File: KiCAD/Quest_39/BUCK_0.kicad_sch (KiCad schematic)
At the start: 26 parts, among them U4 AD626ANZ, U5 INA226, U6 LTM4611EV-PBF, U7 MCP4151-502E/SN

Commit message: Small changes made during schematic review w/ Joost
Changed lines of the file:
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@@
   (junction (at 322.58 137.16) (diameter 0) (color 0 0 0 0)
   )
-  (junction (at 322.58 180.34) (diameter 0) (color 0 0 0 0)
-  )
   (junction (at 236.22 215.9) (diameter 0) (color 0 0 0 0)
   )
@@
   (junction (at 166.37 50.8) (diameter 0) (color 0 0 0 0)
   )
-  (junction (at 322.58 68.58) (diameter 0) (color 0 0 0 0)
-  )
   (junction (at 322.58 101.6) (diameter 0) (color 0 0 0 0)
   )
@@
   )
   (junction (at 241.3 215.9) (diameter 0) (color 0 0 0 0)
-  )
-  (junction (at 162.56 215.9) (diameter 0) (color 0 0 0 0)
   )
   (junction (at 200.66 215.9) (diameter 0) (color 0 0 0 0)
@@
     (stroke (width 0) (type default) (color 0 0 0 0))
   )
-  (wire (pts (xy 322.58 68.58) (xy 322.58 66.04))
-    (stroke (width 0) (type default) (color 0 0 0 0))
-  )
   (wire (pts (xy 25.4 69.85) (xy 62.23 69.85))
     (stroke (width 0) (type default) (color 0 0 0 0))
@@
     (stroke (width 0) (type default) (color 0 0 0 0))
   )
-  (wire (pts (xy 322.58 180.34) (xy 322.58 177.8))
+  (wire (pts (xy 130.81 152.4) (xy 130.81 154.94))
     (stroke (width 0) (type default) (color 0 0 0 0))
   )
@@
     (stroke (width 0) (type default) (color 0 0 0 0))
   )
-  (wire (pts (xy 130.81 215.9) (xy 162.56 215.9))
-    (stroke (width 0) (type default) (color 0 0 0 0))
-  )
   (wire (pts (xy 322.58 132.08) (xy 322.58 134.62))
     (stroke (width 0) (type default) (color 0 0 0 0))
@@
     (stroke (width 0) (type default) (color 0 0 0 0))
   )
-  (wire (pts (xy 356.87 215.9) (xy 397.51 215.9))
+  (wire (pts (xy 356.87 215.9) (xy 400.05 215.9))
     (stroke (width 0) (type default) (color 0 0 0 0))
   )
@@
     (stroke (width 0) (type default) (color 0 0 0 0))
   )
+  (wire (pts (xy 130.81 154.94) (xy 129.54 154.94))
+    (stroke (width 0) (type default) (color 0 0 0 0))
+  )
   (wire (pts (xy 271.78 215.9) (xy 269.24 215.9))
     (stroke (width 0) (type default) (color 0 0 0 0))
@@
     (stroke (width 0) (type default) (color 0 0 0 0))
   )
-  (wire (pts (xy 130.81 152.4) (xy 130.81 215.9))
-    (stroke (width 0) (type default) (color 0 0 0 0))
-  )
   (polyline (pts (xy 351.79 219.71) (xy 278.13 219.71))
     (stroke (width 0) (type default) (color 0 0 0 0))
@@
     (stroke (width 0) (type default) (color 0 0 0 0))
   )
-  (wire (pts (xy 396.24 172.72) (xy 397.51 172.72))
+  (wire (pts (xy 396.24 172.72) (xy 400.05 172.72))
     (stroke (width 0) (type default) (color 0 0 0 0))
   )
@@
     (effects (font (size 1.27 1.27)) (justify left))
   )
-  (hierarchical_label "NEG" (shape output) (at 397.51 215.9 0)
+  (hierarchical_label "NEG" (shape output) (at 400.05 215.9 0)
     (effects (font (size 1.27 1.27)) (justify left))
+  )
+  (hierarchical_label "NEG" (shape output) (at 129.54 154.94 180)
+    (effects (font (size 1.27 1.27)) (justify right))
   )
   (hierarchical_label "SCK" (shape input) (at 285.75 232.41 180)
@@
     (effects (font (size 1.27 1.27)) (justify right))
   )
-  (hierarchical_label "POS" (shape output) (at 397.51 172.72 0)
+  (hierarchical_label "POS" (shape output) (at 400.05 172.72 0)
     (effects (font (size 1.27 1.27)) (justify left))
   )

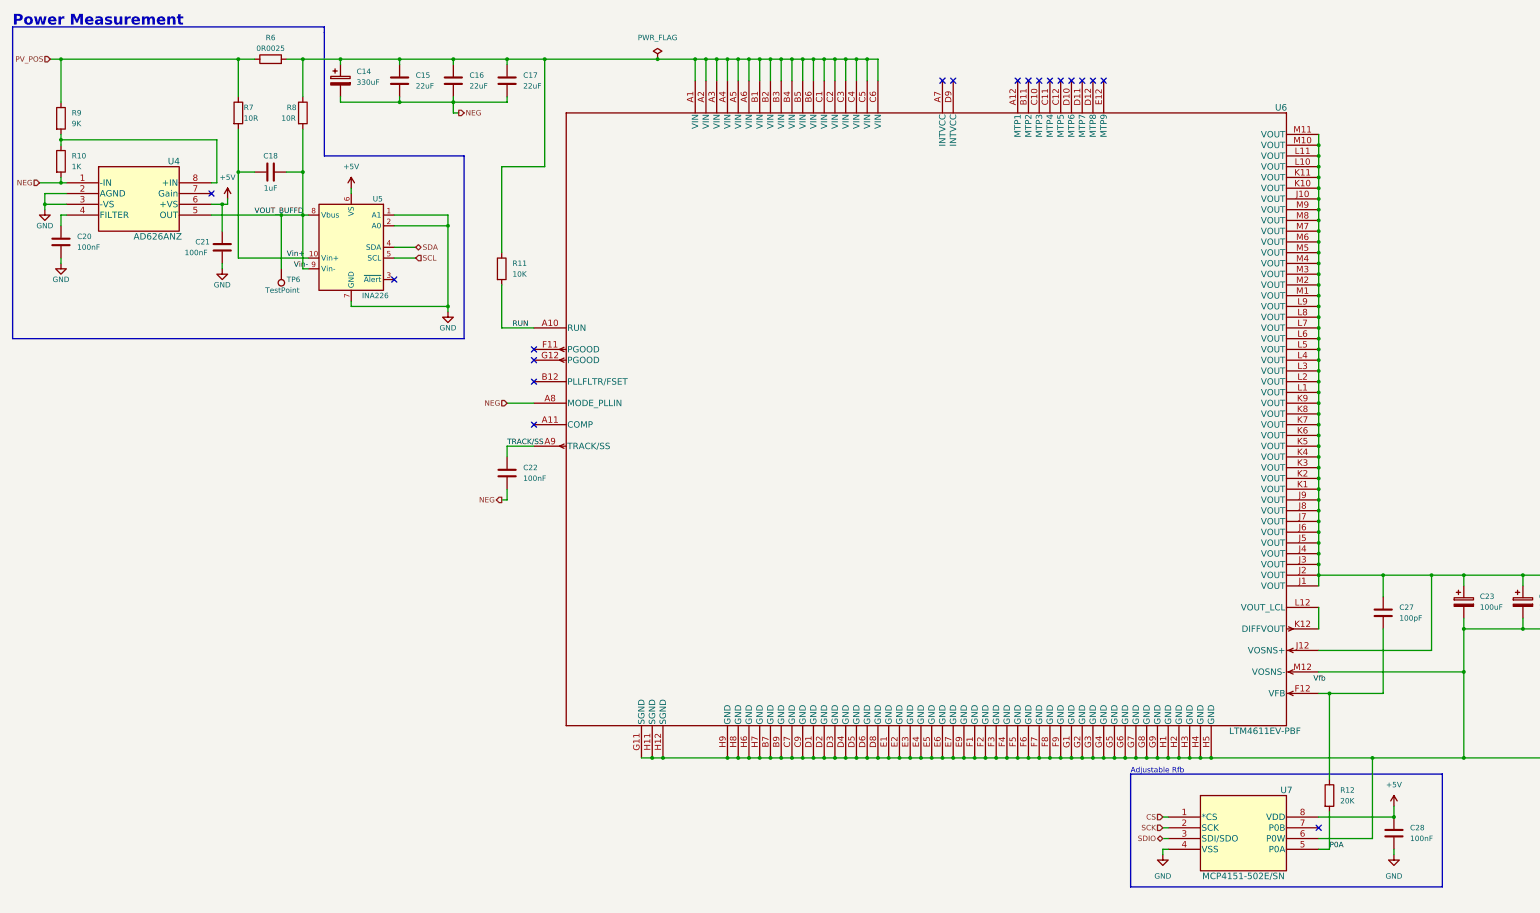
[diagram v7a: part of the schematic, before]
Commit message: Added weak SPI CS pullups to prevent spurious behaviour
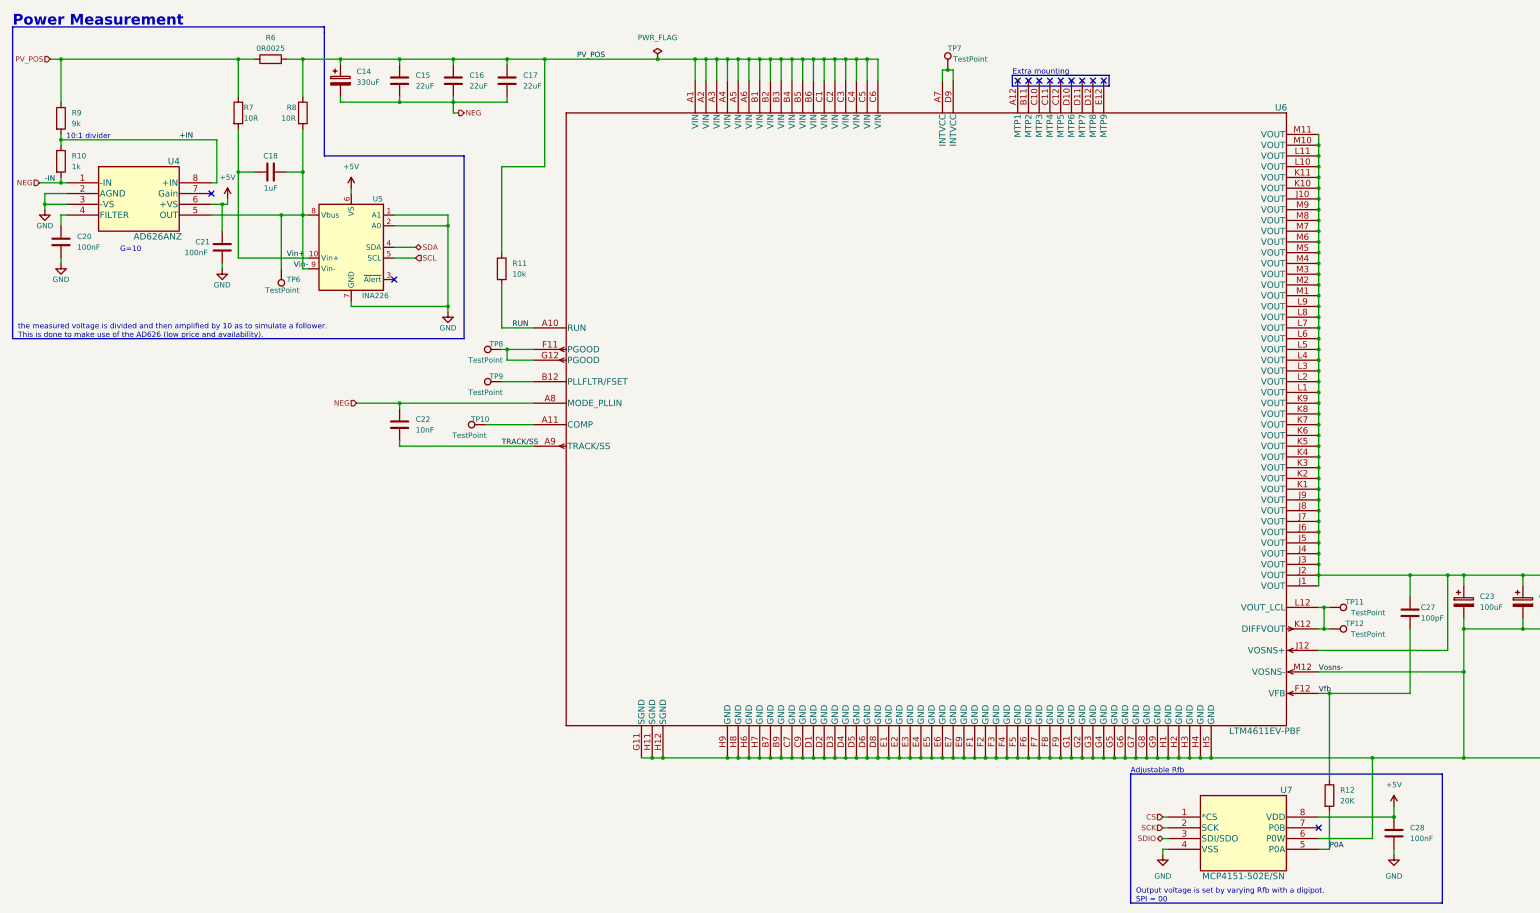
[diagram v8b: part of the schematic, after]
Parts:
- added TP10, TP11, TP12, TP7, TP8, TP9: TestPoint, symbol Connector:TestPoint
- C22: value 100nF -> 10nF
- R10: value 1K -> 1k
- R11: value 10K -> 10k
- R9: value 9K -> 9k
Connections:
- net NEG: now also C22.1; no longer C22.2
- net PV_POS: now also C14.1, C15.1, C16.1, C17.1, R11.1, R6.2, R8.1, U6.A1 (VIN), U6.A2 (VIN), U6.A3 (VIN), U6.A4 (VIN), U6.A5 (VIN), U6.A6 (VIN), U6.B1 (VIN), U6.B2 (VIN), U6.B3 (VIN), U6.B4 (VIN), U6.B5 (VIN), U6.B6 (VIN), U6.C1 (VIN), U6.C2 (VIN), U6.C3 (VIN), U6.C4 (VIN), U6.C5 (VIN), U6.C6 (VIN)
- net TRACK/SS: now also C22.2; no longer C22.1
- net Vfb: now also C27.2, R12.1, U6.F12 (VFB)
- net +IN: now reaches R10.1, R9.2, U4.8 (+IN)
- net at U6.A11 (COMP): now also TP10.1
- net at U6.A7 (INTVCC): now also U6.D9 (INTVCC), TP7.1
- net at U6.B12 (PLLFLTR/FSET): now also TP9.1
- net at U6.F11 (PGOOD): now also U6.G12 (PGOOD), TP8.1
- net at U6.K12 (DIFFVOUT), U6.L12 (VOUT_LCL): now also TP11.1, TP12.1
- net VOUT_BUFFD renamed Vin-
- no-connect marks 18 -> 12
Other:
- note added: "10:1 divider"
- note added: "Extra mounting"
- note added: "G=10"
- note added: "Output voltage is set by varying Rfb with a digipot. SPI = 00"
- note added: "the measured voltage is divided and then amplified by 10 as to simulate a follower. This is done to make use of the AD626 (low price and availability)."
- moved on the sheet: C22, C27
